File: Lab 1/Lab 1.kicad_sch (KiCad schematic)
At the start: 50 parts, among them K1 Fujitsu_FTR-LYCA005x, K10 Fujitsu_FTR-LYCA005x, K11 Fujitsu_FTR-LYCA005x, K12 Fujitsu_FTR-LYCA005x, K13 Fujitsu_FTR-LYCA005x, K14 Fujitsu_FTR-LYCA005x, K15 Fujitsu_FTR-LYCA005x, K2 Fujitsu_FTR-LYCA005x, K3 Fujitsu_FTR-LYCA005x, K4 Fujitsu_FTR-LYCA005x, K5 Fujitsu_FTR-LYCA005x, K6 Fujitsu_FTR-LYCA005x, K7 Fujitsu_FTR-LYCA005x, K8 Fujitsu_FTR-LYCA005x, K9 Fujitsu_FTR-LYCA005x, M1 Motor_DC, M2 Motor_DC, M3 Motor_DC, SW1 SW_Push, SW10 SW_Nidec_CAS-120A1, SW11 SW_Nidec_CAS-120A1, SW12 SW_Nidec_CAS-120A1, SW13 SW_Push, SW2 SW_Push_Open, SW3 SW_Push, SW4 SW_Push_Open, SW5 SW_Push, SW6 SW_Push, SW7 SW_Push, SW8 SW_Push, SW9 SW_Nidec_CAS-120A1

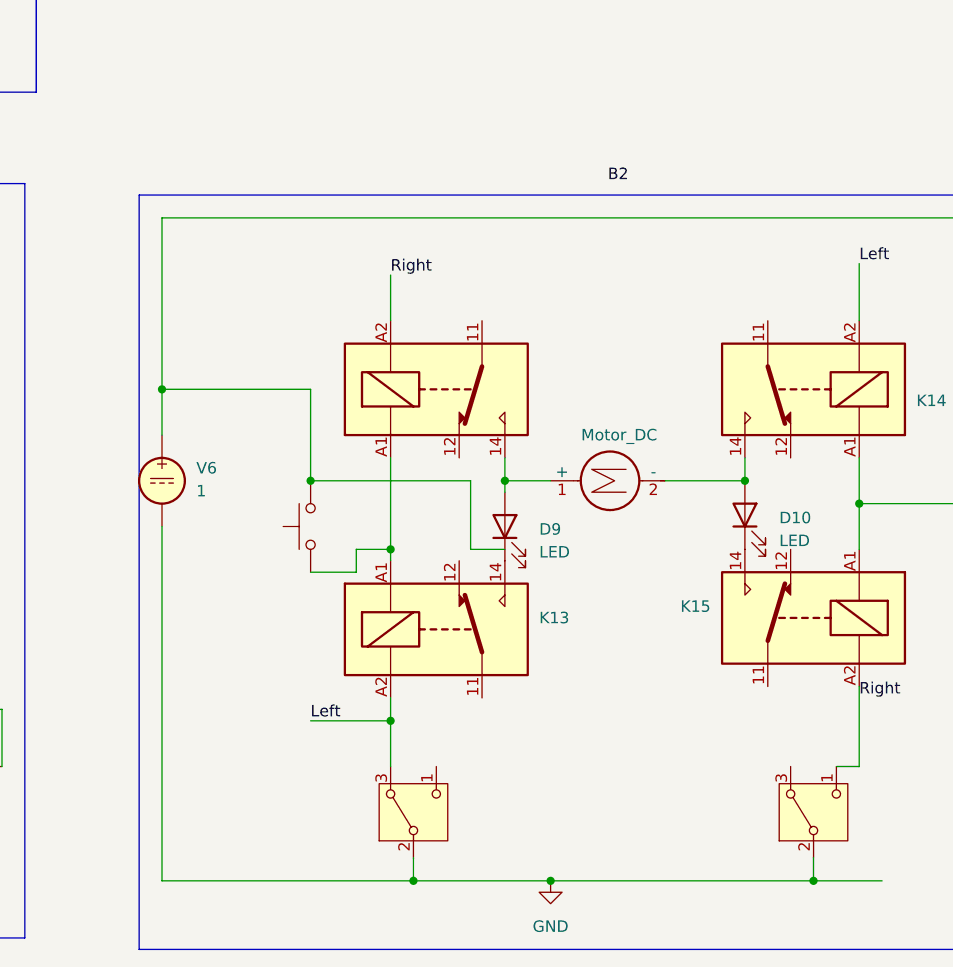
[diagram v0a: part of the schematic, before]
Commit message: Upgrade KiCad to v9, fix folder structure
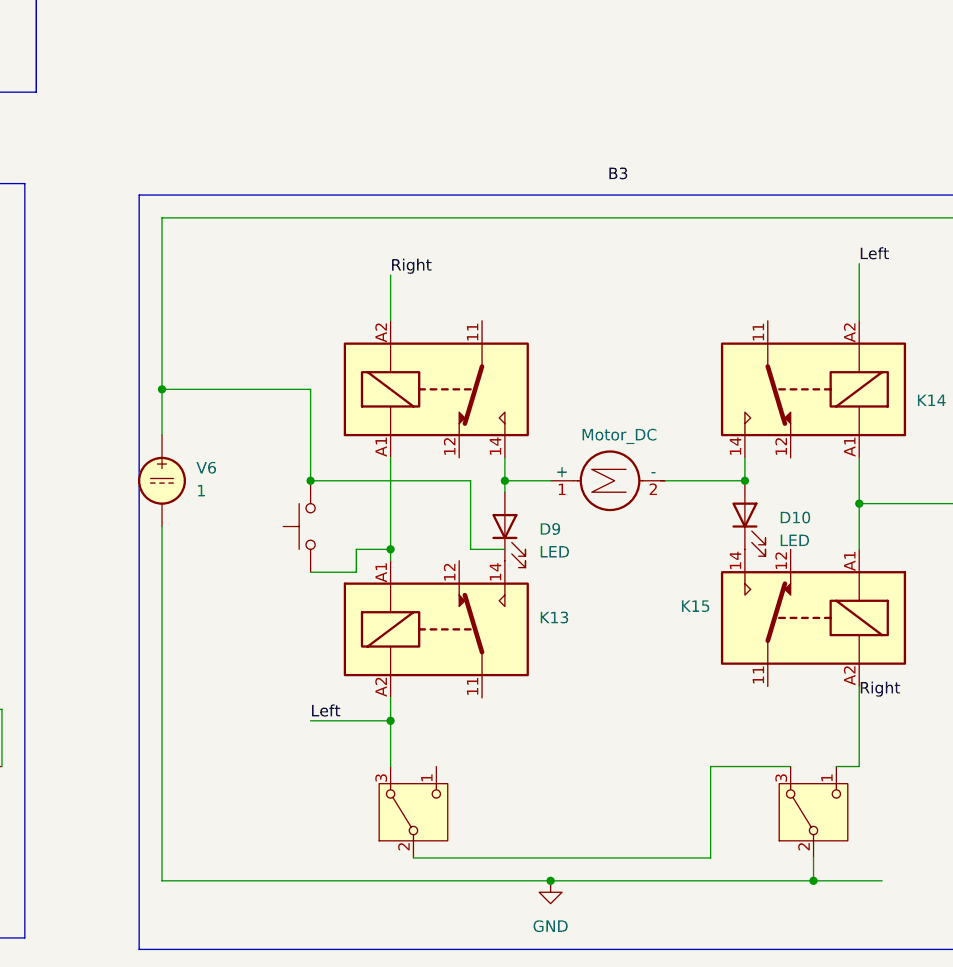
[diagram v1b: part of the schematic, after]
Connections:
- net GND: no longer SW10.2 (B)
- net at SW12.3 (A): now also SW10.2 (B)
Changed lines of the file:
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@@
 (kicad_sch
-	(version 20231120)
+	(version 20250114)
 	(generator "eeschema")
-	(generator_version "8.0")
+	(generator_version "9.0")
 	(paper "A3")
+	(rectangle
+		(start 153.67 17.78)
+		(end 233.68 72.39)
+		(stroke
+			(width 0)
+			(type default)
+		)
+		(fill
+			(type none)
+		)
+	)
+	(rectangle
+		(start 86.36 17.78)
+		(end 149.86 72.39)
+		(stroke
+			(width 0)
+			(type default)
+		)
+		(fill
+			(type none)
+		)
+	)
+	(rectangle
+		(start 124.46 82.55)
+		(end 232.41 166.37)
+		(stroke
+			(width 0)
+			(type default)
+		)
+		(fill
+			(type none)
+		)
+	)
+	(rectangle
+		(start 19.05 17.78)
+		(end 83.82 72.39)
+		(stroke
+			(width 0)
+			(type default)
+		)
+		(fill
+			(type none)
+		)
+	)
+	(rectangle
+		(start 245.11 83.82)
+		(end 356.87 167.64)
+		(stroke
+			(width 0)
+			(type default)
+		)
+		(fill
+			(type none)
+		)
+	)
+	(rectangle
+		(start 16.51 82.55)
+		(end 116.84 156.21)
+		(stroke
+			(width 0)
+			(type default)
+		)
+		(fill
+			(type none)
+		)
+	)
 	(junction
 		(at 154.94 158.75)
@@
 	)
 	(junction
-		(at 275.59 160.02)
-		(diameter 0)
-		(color 0 0 0 0)
-	)
-	(junction
 		(at 88.9 151.13)
 		(diameter 0)
@@
 	(wire
 		(pts
-			(xy 177.8 62.23) (xy 177.8 64.77)
+			(xy 308.61 147.32) (xy 317.5 147.32)
 		)
 		(stroke
@@
 	(wire
 		(pts
-			(xy 110.49 26.67) (xy 120.65 26.67)
+			(xy 177.8 62.23) (xy 177.8 64.77)
 		)
 		(stroke
@@
 	(wire
 		(pts
-			(xy 177.8 64.77) (xy 187.96 64.77)
+			(xy 110.49 26.67) (xy 120.65 26.67)
 		)
 		(stroke
@@
 	(wire
 		(pts
-			(xy 162.56 85.09) (xy 194.31 85.09)
+			(xy 177.8 64.77) (xy 187.96 64.77)
 		)
 		(stroke
@@
 	(wire
 		(pts
-			(xy 162.56 85.09) (xy 162.56 96.52)
+			(xy 162.56 85.09) (xy 194.31 85.09)
 		)
 		(stroke
@@
 	(wire
 		(pts
-			(xy 275.59 157.48) (xy 275.59 160.02)
+			(xy 162.56 85.09) (xy 162.56 96.52)
 		)
 		(stroke
@@
 	(wire
 		(pts
-			(xy 247.65 160.02) (xy 275.59 160.02)
+			(xy 247.65 160.02) (xy 290.83 160.02)
 		)
 		(stroke
@@
 	(wire
 		(pts
-			(xy 275.59 160.02) (xy 290.83 160.02)
-		)
-		(stroke
-			(width 0)
-			(type default)
-		)
-	)
-	(wire
-		(pts
 			(xy 99.06 113.03) (xy 99.06 118.11)
 		)
@@
 	(wire
 		(pts
+			(xy 275.59 157.48) (xy 308.61 157.48)
+		)
+		(stroke
+			(width 0)
+			(type default)
+		)
+	)
+	(wire
+		(pts
 			(xy 57.15 151.13) (xy 64.77 151.13)
 		)
@@
 	(wire
 		(pts
+			(xy 308.61 157.48) (xy 308.61 147.32)
+		)
+		(stroke
+			(width 0)
+			(type default)
+		)
+	)
+	(wire
+		(pts
 			(xy 152.4 116.84) (xy 152.4 123.19)
 		)
@@
 		)
 	)
-	(rectangle
-		(start 153.67 17.78)
-		(end 233.68 72.39)
-		(stroke
-			(width 0)
-			(type default)
-		)
-		(fill
-			(type none)
-		)
-	)
-	(rectangle
-		(start 86.36 17.78)
-		(end 149.86 72.39)
-		(stroke
-			(width 0)
-			(type default)
-		)
-		(fill
-			(type none)
-		)
-	)
-	(rectangle
-		(start 124.46 82.55)
-		(end 232.41 166.37)
-		(stroke
-			(width 0)
-			(type default)
-		)
-		(fill
-			(type none)
-		)
-	)
-	(rectangle
-		(start 19.05 17.78)
-		(end 83.82 72.39)
-		(stroke
-			(width 0)
-			(type default)
-		)
-		(fill
-			(type none)
-		)
-	)
-	(rectangle
-		(start 245.11 83.82)
-		(end 356.87 167.64)
-		(stroke
-			(width 0)
-			(type default)
-		)
-		(fill
-			(type none)
-		)
-	)
-	(rectangle
-		(start 16.51 82.55)
-		(end 116.84 156.21)
-		(stroke
-			(width 0)
-			(type default)
-		)
-		(fill
-			(type none)
-		)
-	)
 	(label "Left"
 		(at 325.12 91.44 0)
-		(fields_autoplaced yes)
 		(effects
 			(font
@@
 	(label "Left"
 		(at 99.06 95.25 0)
-		(fields_autoplaced yes)
 		(effects
 			(font
@@
 	(label "B2"
 		(at 93.98 76.2 0)
-		(fields_autoplaced yes)
 		(effects
 			(font
@@
 	(label "Left"
 		(at 264.16 142.24 0)
-		(fields_autoplaced yes)
 		(effects
 			(font
@@
 	(label "Right"
 		(at 46.99 92.71 0)
-		(fields_autoplaced yes)
 		(effects
 			(font
@@
 	(label "Right"
 		(at 325.12 139.7 0)
-		(fields_autoplaced yes)
 		(effects
 			(font
@@
 	(label "Right"
 		(at 273.05 92.71 0)
-		(fields_autoplaced yes)
 		(effects
 			(font
@@
 	(label "B1"
 		(at 67.31 80.01 0)
-		(fields_autoplaced yes)
 		(effects
 			(font
@@
 		)
 	)
-	(label "B2"
+	(label "B3"
 		(at 297.18 82.55 0)
-		(fields_autoplaced yes)
 		(effects
 			(font
@@
 	(label "Left"
 		(at 40.64 139.7 0)
-		(fields_autoplaced yes)
 		(effects
 			(font
@@
 	(label "Left"
 		(at 146.05 138.43 0)
-		(fields_autoplaced yes)
 		(effects
 			(font
@@
 	(label "Right"
 		(at 101.6 139.7 0)
-		(fields_autoplaced yes)
 		(effects
 			(font
@@
 	(label "Right"
 		(at 152.4 91.44 0)
-		(fields_autoplaced yes)
 		(effects
 			(font
@@
 	(label "A2"
 		(at 39.37 16.51 0)
-		(fields_autoplaced yes)
 		(effects
 			(font
@@
 	(label "A3"
 		(at 106.68 16.51 0)
-		(fields_autoplaced yes)
 		(effects
 			(font
@@
 	(label "B2"
 		(at 176.53 81.28 0)
-		(fields_autoplaced yes)
 		(effects
 			(font
@@
 	(label "Right"
 		(at 207.01 138.43 0)
-		(fields_autoplaced yes)
 		(effects
 			(font
@@
 	(label "Left"
 		(at 204.47 93.98 0)
-		(fields_autoplaced yes)
 		(effects
 			(font
@@
 	(label "A4"
 		(at 173.99 16.51 0)
-		(fields_autoplaced yes)
 		(effects
 			(font
@@
 		)
 	)
+	(embedded_fonts no)
 )
